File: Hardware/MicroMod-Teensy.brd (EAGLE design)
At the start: 22 x 22.8 mm, 80 parts, among them J1 MICROMOD-2222, Q1 20V/4.2A/52mΩ/1.4W, Q2 20V/0.2A/8MHz/1.2Ω/1Vth, U1 IMXRT1062DV10X10, U3 MKL02Z32VFG4, U4 W25QXX128MBIT-6X5, Y1 32.768kHz, Y2 24MHz

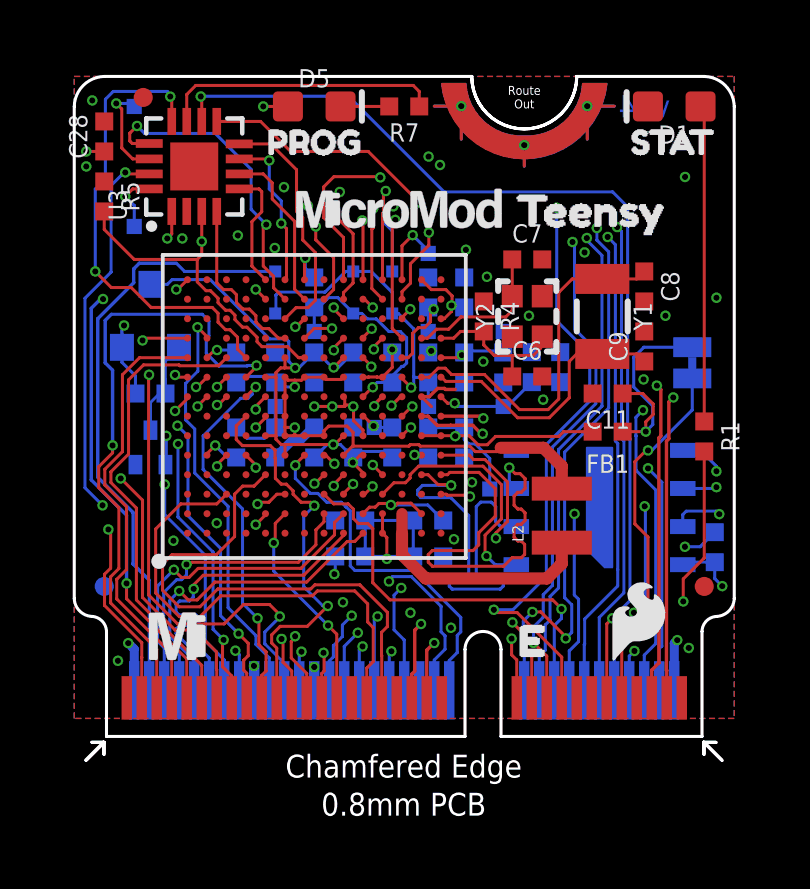
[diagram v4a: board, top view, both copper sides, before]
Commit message: Switch layers 2/15 to put ground under xtals. Increase GND plane on layer 15.
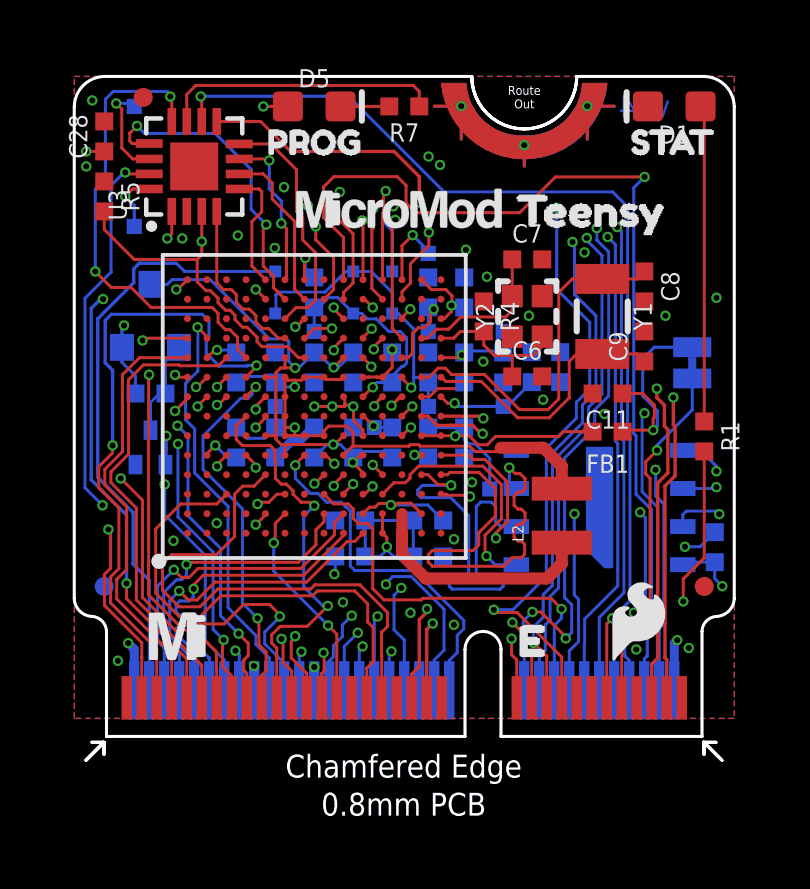
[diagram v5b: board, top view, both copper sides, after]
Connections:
- net N$31 renamed 32KHZ_2
- net N$32 renamed 32KHZ_1
- net N$4 renamed 24MHZ_1
- net N$5 renamed 24MHZ_2
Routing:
- net GND: track 20.8 -> 20.3 mm, vias 37 -> 36
- net GPIO/27/A13: track 33.7 -> 33.5 mm, vias 3 -> 1
- added copper zone on layer 15, net 3.3V
- removed copper zone on layer 2, net 3.3V

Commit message: Increase TP size and relocate to more open areas
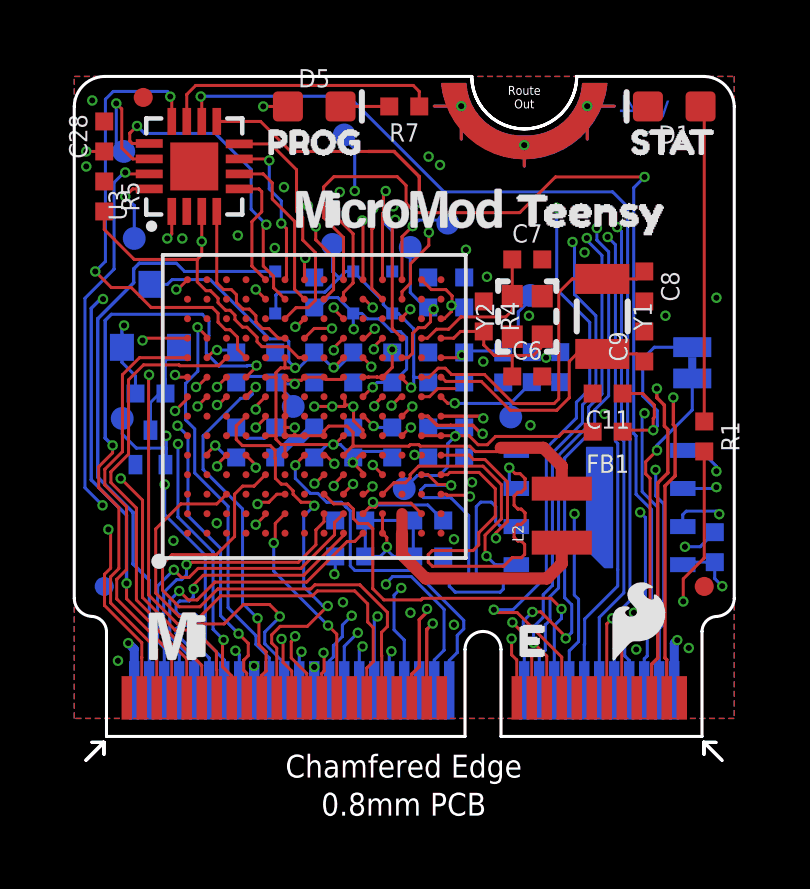
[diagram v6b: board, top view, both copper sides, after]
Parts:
- TP1, TP10, TP11, TP2, TP3, TP4, TP5, TP6, TP7, TP8, TP9: device SparkFun-Connectors:PAD.02X.02 -> SparkFun-Connectors:PAD.03X.03
- moved TP2 8.41 mm to (1.60, 10.6)
- moved TP11 6.63 mm to (9.00, 20.0)
- moved TP4 6.28 mm to (8.61, 16.4)
- moved TP5 2.86 mm to (11.2, 16.3)
- moved TP3 2.85 mm to (11.0, 8.25)
- moved TP9 1.54 mm to (1.65, 19.5)
- moved TP6 1.50 mm to (15.2, 14.7)
- moved TP1 1.20 mm to (12.4, 17.1)
- moved TP10 0.60 mm to (7.30, 11.0)
- moved TP7 0.43 mm to (14.6, 10.6)
- moved TP8 0.40 mm to (2.00, 16.6)
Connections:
- net 32KHZ_TEST: now also TP1.P$1; no longer TP1.1
- net NVCC_PLL: now also TP6.P$1; no longer TP6.1
- net PMIC: now also TP2.P$1; no longer TP2.1
- net SWD_CLK: now also TP9.P$1; no longer TP9.1
- net SWD_DIO: now also TP8.P$1; no longer TP8.1
- net VCC: now also TP3.P$1; no longer TP3.1
- net VDD_HIGH_CAP: now also TP7.P$1; no longer TP7.1
- net VDD_SNVS_CAP: now also TP5.P$1; no longer TP5.1
- net VDD_SNVS_IN: now also TP4.P$1; no longer TP4.1
- net VDD_SOC_IN: now also TP10.P$1; no longer TP10.1
- net VDD_USB_CAP: now also TP11.P$1; no longer TP11.1
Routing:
- net VDD_USB_CAP: track 7.47 -> 13.9 mm, vias 1 -> 3
- net PMIC: track 10.2 -> 12.5 mm
- net NVCC_PLL: track 2.89 -> 4.47 mm
- net VDD_SNVS_CAP: track 3.31 -> 4.81 mm
- net SWD_CLK: track 35.6 -> 36.7 mm
- net 32KHZ_TEST: track 2.46 -> 3.23 mm
- net GND: track 20.3 -> 20.4 mm, vias 36 -> 37
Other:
- board text removed: "All Test Point Measurements in mm"
- board text removed: "TP is 0.5x0.5mm"
- board text removed: "TP1"
- board text removed: "TP10"
- board text removed: "TP11"
- board text removed: "TP2"
- board text removed: "TP3"
- board text removed: "TP4"
- board text removed: "TP5"
- board text removed: "TP6"
- board text removed: "TP7"
- board text removed: "TP8"
- board text removed: "TP9"
- board text removed: "Viewing Bottom of Board"

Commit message: High freq trace length matching
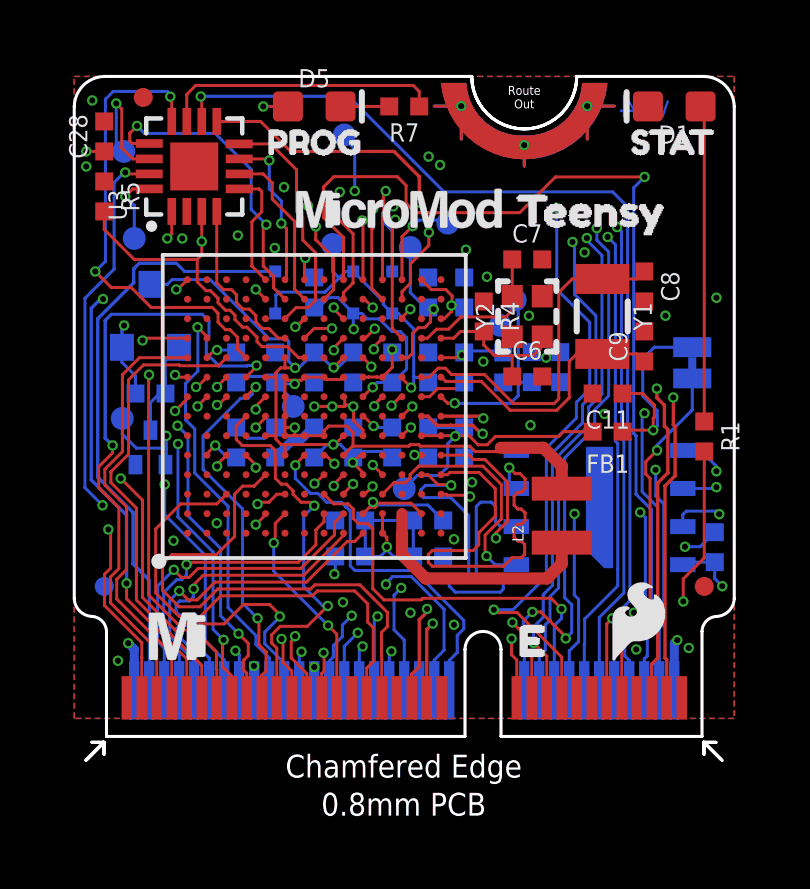
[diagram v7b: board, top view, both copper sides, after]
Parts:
- moved TP7 3.90 mm to (14.7, 14.5)
- moved TP6 1.41 mm to (14.2, 13.7)
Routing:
- net VDD_HIGH_CAP: track 4.82 -> 7.41 mm
- net SWD_DIO: track 32.9 -> 35.0 mm
- net SWD_CLK: track 36.7 -> 38.7 mm
- net NVCC_PLL: track 4.47 -> 3.14 mm
- net QSPI-CLK: track 15.6 -> 14.8 mm
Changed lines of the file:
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@@
 <grid distance="1" unitdist="mm" unit="mm" style="lines" multiple="1" display="yes" altdistance="0.05" altunitdist="mm" altunit="mm"/>
 <layers>
-<layer number="1" name="Top" color="4" fill="1" visible="no" active="yes"/>
+<layer number="1" name="Top" color="4" fill="1" visible="yes" active="yes"/>
 <layer number="2" name="Vert-GND" color="1" fill="3" visible="no" active="yes"/>
 <layer number="15" name="Horz-3V3" color="4" fill="6" visible="no" active="yes"/>
-<layer number="16" name="Bottom" color="1" fill="1" visible="yes" active="yes"/>
+<layer number="16" name="Bottom" color="1" fill="1" visible="no" active="yes"/>
 <layer number="17" name="Pads" color="2" fill="1" visible="yes" active="yes"/>
 <layer number="18" name="Vias" color="2" fill="1" visible="yes" active="yes"/>
@@
 <layer number="21" name="tPlace" color="16" fill="1" visible="no" active="yes"/>
 <layer number="22" name="bPlace" color="14" fill="1" visible="no" active="yes"/>
-<layer number="23" name="tOrigins" color="15" fill="1" visible="no" active="yes"/>
-<layer number="24" name="bOrigins" color="15" fill="1" visible="yes" active="yes"/>
+<layer number="23" name="tOrigins" color="15" fill="1" visible="yes" active="yes"/>
+<layer number="24" name="bOrigins" color="15" fill="1" visible="no" active="yes"/>
 <layer number="25" name="tNames" color="7" fill="1" visible="no" active="yes"/>
 <layer number="26" name="bNames" color="7" fill="1" visible="no" active="yes"/>
@@
 </element>
 <element name="TP5" library="SparkFun-Connectors" package="PAD.03X.03" value="" x="11.2" y="16.29" smashed="yes" rot="MR0"/>
-<element name="TP6" library="SparkFun-Connectors" package="PAD.03X.03" value="" x="15.2" y="14.69" smashed="yes" rot="MR0"/>
-<element name="TP7" library="SparkFun-Connectors" package="PAD.03X.03" value="" x="14.55" y="10.64" smashed="yes" rot="MR0"/>
+<element name="TP6" library="SparkFun-Connectors" package="PAD.03X.03" value="" x="14.2" y="13.69" smashed="yes" rot="MR0"/>
+<element name="TP7" library="SparkFun-Connectors" package="PAD.03X.03" value="" x="14.7" y="14.54" smashed="yes" rot="MR0"/>
 <element name="FD1" library="SparkFun-Aesthetics" package="FIDUCIAL-MICRO" value="FIDUCIALUFIDUCIAL" x="21" y="4.99" smashed="yes"/>
 <element name="FD2" library="SparkFun-Aesthetics" package="FIDUCIAL-MICRO" value="FIDUCIALUFIDUCIAL" x="2.3" y="21.29" smashed="yes"/>
@@
 <wire x1="14.25" y1="12.84" x2="13.05" y2="12.84" width="0.1016" layer="16"/>
 <wire x1="13.05" y1="12.84" x2="13" y2="12.79" width="0.1016" layer="16"/>
-<wire x1="15.2" y1="14.69" x2="15.2" y2="14.54" width="0.1016" layer="16"/>
-<wire x1="15.2" y1="14.54" x2="14.8" y2="14.14" width="0.1016" layer="16"/>
-<wire x1="14.8" y1="14.14" x2="14.8" y2="13.64" width="0.1016" layer="16"/>
-<wire x1="14.8" y1="13.64" x2="14.3" y2="13.14" width="0.1016" layer="16"/>
-<wire x1="14.3" y1="13.14" x2="14.3" y2="12.79" width="0.1016" layer="16"/>
+<wire x1="14.3" y1="12.79" x2="14.3" y2="13.59" width="0.1016" layer="16"/>
+<wire x1="14.3" y1="13.59" x2="14.2" y2="13.69" width="0.1016" layer="16"/>
 </signal>
 <signal name="VDD_HIGH_CAP">
@@
 <via x="12.681" y="11.098" extent="1-16" drill="0.2"/>
 <wire x1="12.681" y1="11.098" x2="12.689" y2="11.09" width="0.1016" layer="16"/>
-<wire x1="14.1" y1="11.09" x2="14" y2="11.09" width="0.1016" layer="16"/>
-<wire x1="14" y1="11.09" x2="12.689" y2="11.09" width="0.1016" layer="16"/>
+<wire x1="12.689" y1="11.09" x2="14.54" y2="11.09" width="0.1016" layer="16"/>
 <wire x1="15.25" y1="11.8" x2="16.2" y2="11.8" width="0.1016" layer="16"/>
-<wire x1="15.25" y1="11.8" x2="14.55" y2="11.1" width="0.1016" layer="16"/>
-<wire x1="14.55" y1="11.1" x2="14.55" y2="10.64" width="0.1016" layer="16"/>
-<wire x1="14.1" y1="11.09" x2="14.54" y2="11.09" width="0.1016" layer="16"/>
-<wire x1="14.54" y1="11.09" x2="14.55" y2="11.1" width="0.1016" layer="16"/>
+<wire x1="14.54" y1="11.09" x2="14.7976" y2="11.3476" width="0.1016" layer="16"/>
+<wire x1="14.7976" y1="11.3476" x2="14.7976" y2="11.8" width="0.1016" layer="16"/>
+<wire x1="15.25" y1="11.8" x2="14.7976" y2="11.8" width="0.1016" layer="16"/>
+<wire x1="14.7976" y1="14.4424" x2="14.7" y2="14.54" width="0.1016" layer="16"/>
+<wire x1="14.7976" y1="11.8" x2="14.7976" y2="14.4424" width="0.1016" layer="16"/>
 </signal>
 <signal name="BOOTMODE0">
@@
 <wire x1="11.35" y1="8.4" x2="10.59" y2="8.4" width="0.1016" layer="15"/>
 <wire x1="10.59" y1="8.4" x2="9.95" y2="9.04" width="0.1016" layer="15"/>
-<wire x1="19.7088" y1="6.604" x2="20.45" y2="7.3452" width="0.1016" layer="15"/>
-<wire x1="20.45" y1="8.4" x2="20.6" y2="8.55" width="0.1016" layer="15"/>
-<wire x1="20.8" y1="8.55" x2="20.6" y2="8.55" width="0.1016" layer="15"/>
-<wire x1="20.45" y1="7.3452" x2="20.45" y2="8.4" width="0.1016" layer="15"/>
-<wire x1="21.4048" y1="8.3" x2="21.05" y2="8.3" width="0.1016" layer="15"/>
-<wire x1="21.05" y1="8.3" x2="20.8" y2="8.55" width="0.1016" layer="15"/>
+<wire x1="19.7088" y1="6.604" x2="21.4048" y2="8.3" width="0.1016" layer="15"/>
 </signal>
 <signal name="QSPI0">
@@
 <wire x1="11.5301" y1="19.59955" x2="1.650675" y2="19.59955" width="0.1016" layer="15"/>
 <wire x1="14.605" y1="3.7913" x2="14.605" y2="4.05461875" width="0.1143" layer="2"/>
-<wire x1="14.605" y1="4.05461875" x2="15.36485" y2="4.81446875" width="0.1143" layer="2"/>
-<wire x1="15.36485" y1="4.81446875" x2="15.36485" y2="9.64433125" width="0.1143" layer="2"/>
-<wire x1="15.36485" y1="9.64433125" x2="14.56485" y2="10.44433125" width="0.1143" layer="2"/>
-<wire x1="12.33074375" y1="19.37495" x2="11.8673" y2="19.37495" width="0.1143" layer="2"/>
-<wire x1="14.56485" y1="10.44433125" x2="14.56485" y2="17.14084375" width="0.1143" layer="2"/>
-<wire x1="14.56485" y1="17.14084375" x2="12.33074375" y2="19.37495" width="0.1143" layer="2"/>
+<wire x1="14.605" y1="4.05461875" x2="17.31485" y2="6.76446875" width="0.1143" layer="2"/>
+<wire x1="12.98074375" y1="19.37495" x2="11.8673" y2="19.37495" width="0.1143" layer="2"/>
+<wire x1="17.31485" y1="6.76446875" x2="17.31485" y2="15.04084375" width="0.1143" layer="2"/>
+<wire x1="17.31485" y1="15.04084375" x2="12.98074375" y2="19.37495" width="0.1143" layer="2"/>
 <contactref element="J1" pad="21"/>
 <wire x1="15.25" y1="1.275" x2="15.25" y2="2.64" width="0.1016" layer="1"/>
@@
 <wire x1="14.578" y1="3.25" x2="14.25420625" y2="3.57379375" width="0.1143" layer="2"/>
 <wire x1="14.25420625" y1="3.57379375" x2="14.25420625" y2="4.00915625" width="0.1143" layer="2"/>
-<wire x1="14.34895" y1="16.88305" x2="12.192" y2="19.04" width="0.1143" layer="2"/>
-<wire x1="15.14895" y1="4.9039" x2="15.14895" y2="9.5549" width="0.1143" layer="2"/>
-<wire x1="14.34895" y1="10.3549" x2="14.34895" y2="16.88305" width="0.1143" layer="2"/>
-<wire x1="14.25420625" y1="4.00915625" x2="15.14895" y2="4.9039" width="0.1143" layer="2"/>
-<wire x1="15.14895" y1="9.5549" x2="14.34895" y2="10.3549" width="0.1143" layer="2"/>
+<wire x1="17.09895" y1="14.93305" x2="12.992" y2="19.04" width="0.1143" layer="2"/>
+<wire x1="12.992" y1="19.04" x2="12.192" y2="19.04" width="0.1143" layer="2"/>
+<wire x1="17.09895" y1="6.8539" x2="17.09895" y2="14.93305" width="0.1143" layer="2"/>
+<wire x1="14.25420625" y1="4.00915625" x2="17.09895" y2="6.8539" width="0.1143" layer="2"/>
 <contactref element="J1" pad="23"/>
 <wire x1="14.75" y1="1.275" x2="14.75" y2="2.54" width="0.1016" layer="1"/>
@@
 <wire x1="19.115825" y1="12.3424" x2="18.51" y2="12.3424" width="0.1143" layer="15"/>
 <wire x1="18.51" y1="12.3424" x2="18.41" y2="12.2424" width="0.1143" layer="15"/>
-<wire x1="18.41" y1="11.34" x2="18.32035" y2="11.25035" width="0.1143" layer="15"/>
-<wire x1="18.32035" y1="11.25035" x2="18.14965" y2="11.25035" width="0.1143" layer="15"/>
-<wire x1="18.14965" y1="11.25035" x2="18.06" y2="11.34" width="0.1143" layer="15"/>
-<wire x1="18.06" y1="11.34" x2="18.06" y2="11.89" width="0.1143" layer="15"/>
+<wire x1="18.41" y1="11.59" x2="18.32035" y2="11.50035" width="0.1143" layer="15"/>
+<wire x1="18.32035" y1="11.50035" x2="18.14965" y2="11.50035" width="0.1143" layer="15"/>
+<wire x1="18.14965" y1="11.50035" x2="18.06" y2="11.59" width="0.1143" layer="15"/>
+<wire x1="18.06" y1="11.59" x2="18.06" y2="11.89" width="0.1143" layer="15"/>
 <wire x1="18.06" y1="11.89" x2="17.96" y2="11.99" width="0.1143" layer="15"/>
 <wire x1="17.81" y1="11.99" x2="17.71" y2="11.89" width="0.1143" layer="15"/>
 <wire x1="19.421" y1="12.037225" x2="19.115825" y2="12.3424" width="0.1143" layer="15"/>
-<wire x1="18.41" y1="12.2424" x2="18.41" y2="11.34" width="0.1143" layer="15"/>
+<wire x1="18.41" y1="12.2424" x2="18.41" y2="11.59" width="0.1143" layer="15"/>
 <wire x1="17.96" y1="11.99" x2="17.81" y2="11.99" width="0.1143" layer="15"/>
 <wire x1="17.71" y1="11.44" x2="17.71" y2="11.89" width="0.1143" layer="15"/>

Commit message: Opening layer 2 for better GND connections
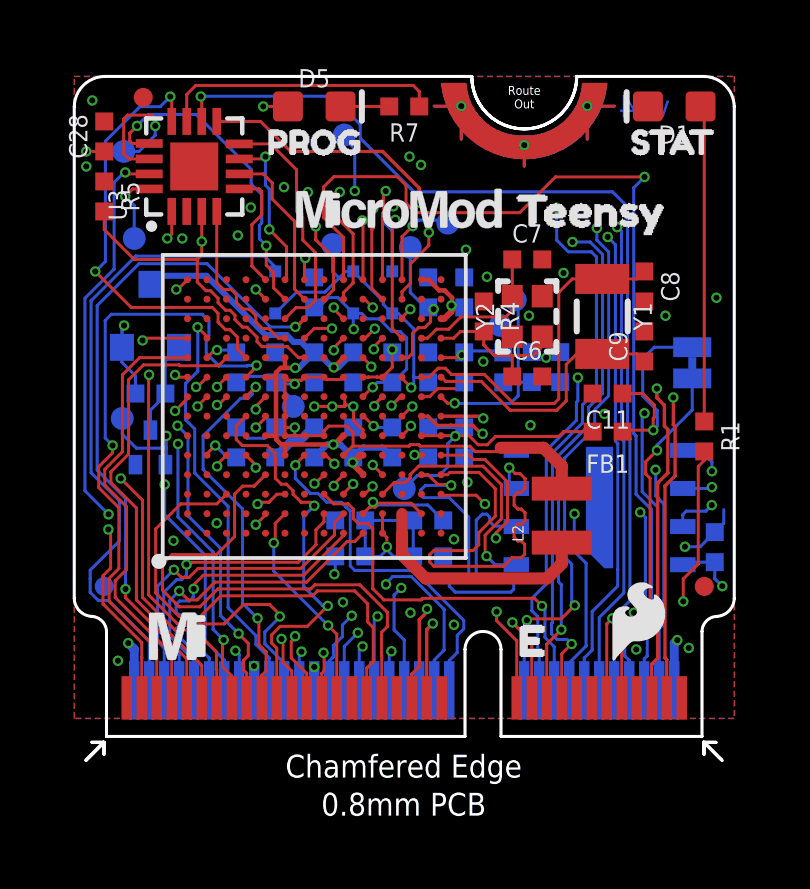
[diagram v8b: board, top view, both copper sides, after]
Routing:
- net RX1/16/A2: track 35.2 -> 18.9 mm
- net SCL1/24/A10: track 26.0 -> 23.5 mm
- net V_BATT: track 20.2 -> 21.9 mm
- net SWD_CLK: track 38.7 -> 37.2 mm
- net TX0/1: track 29.5 -> 28.2 mm
- net TX1/17/A3: track 32.6 -> 31.4 mm
- net SWD_DIO: track 35.0 -> 36.2 mm
- net USB2_D-: track 13.4 -> 12.2 mm
- net USB2_D+: track 13.2 -> 12.1 mm
- net DEBUG_SWO: track 15.7 -> 14.7 mm
- net USB_D-: track 23.7 -> 22.7 mm
- net USB_D+: track 23.7 -> 22.7 mm
- net GND: track 20.4 -> 21.2 mm
- net GPIO/26/A12: track 22.0 -> 22.8 mm, vias 3 -> 2
- net LRCLK/20/A6: track 23.9 -> 24.5 mm
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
